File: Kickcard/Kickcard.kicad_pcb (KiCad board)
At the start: 2 copper layers, 135.3 x 114.8 mm, 74 parts, among them J1 Conn_Side_Expansion, SW1 SW_DIP_x04, SW2 SW_MEC_5E, SW3 SW_MEC_5E, U1 PAL20L8, U2 SST39SF040, U3 SST39SF040, U4 27C400

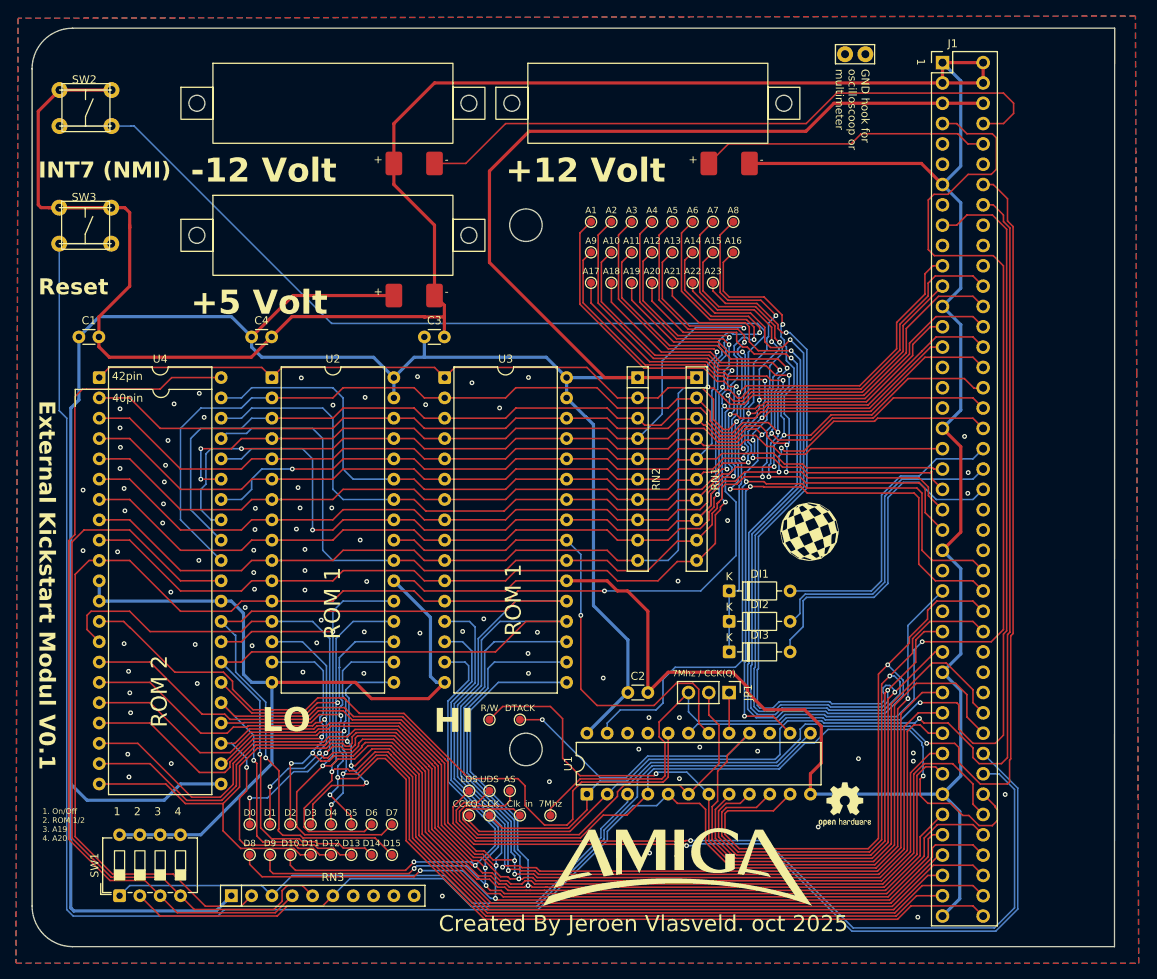
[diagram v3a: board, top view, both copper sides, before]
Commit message: Big Design change
Remove test pins, extra rom and added "expansion" headers, corrected voltmeter footprint dimmensions
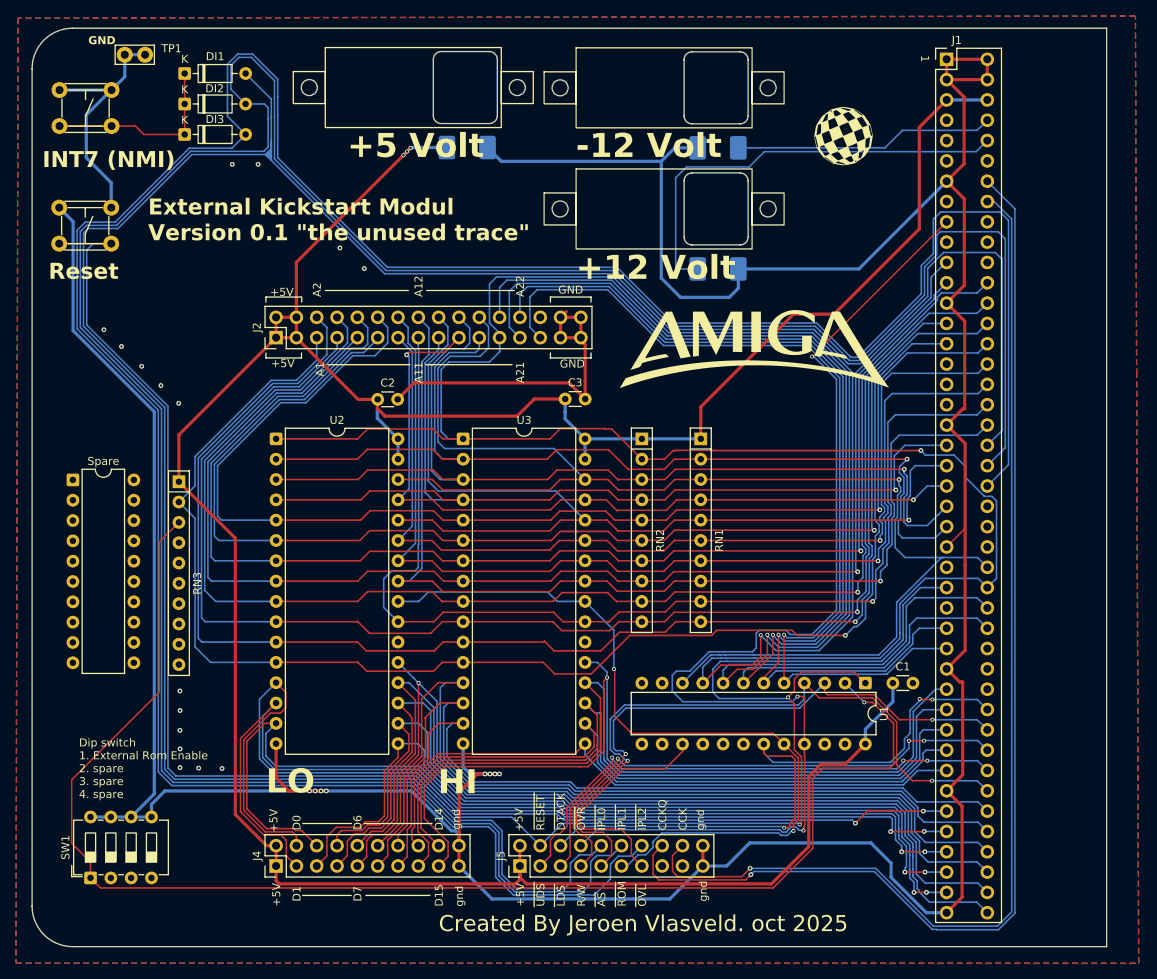
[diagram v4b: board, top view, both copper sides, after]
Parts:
- removed 7Mhz, A1, A10, A11, A12, A13, A14, A15, A16, A17, A18, A19, A2, A20, A21, A22, A23, A3, A4, A5, A6, A7, A8, A9, AS, CCK, CCKQ, Clk_in, D0, D1, D10, D11, D12, D13, D14, D15, D2, D3, D4, D5, D6, D7, D8, D9, DTACK, LDS, R/W, UDS: Conn_01x01, TestPoint:TestPoint_Pad_D1.0mm
- removed C4: 100nf, Capacitor_THT:C_Disc_D3.0mm_W1.6mm_P2.50mm
- removed JP1: Jumper_3_Open, Connector_PinHeader_2.54mm:PinHeader_1x03_P2.54mm_Vertical
- removed REF**: TestPoint_Bridge_Pitch2.54mm_Drill1.0mm, TestPoint:TestPoint_Bridge_Pitch2.54mm_Drill1.0mm
- removed REF**: OSHW-Logo2_7.3x6mm_SilkScreen, Symbol:OSHW-Logo2_7.3x6mm_SilkScreen
- removed U4: 27C400, Package_DIP:DIP-42_W15.24mm
- added J2: Conn_02x16_Odd_Even, Connector_PinHeader_2.54mm:PinHeader_2x16_P2.54mm_Vertical, F.Cu at (106.7, 75.4)
- added J4: Conn_02x10, Connector_PinHeader_2.54mm:PinHeader_2x10_P2.54mm_Vertical, F.Cu at (106.7, 141.5)
- added J5: Conn_02x10, Connector_PinHeader_2.54mm:PinHeader_2x10_P2.54mm_Vertical, F.Cu at (137.2, 141.5)
- added Spare: DIP-20_W7.62mm, Package_DIP:DIP-20_W7.62mm, F.Cu at (81.3, 93.2)
- added TP1: Conn_01x01, TestPoint:TestPoint_Bridge_Pitch2.54mm_Drill1.0mm, F.Cu at (87.8, 40.1)
- U1: value PAL20L8 -> GAL22v10
- moved C1 110.6 mm to (183.8, 118.6)
- moved DI1 93.9 mm to (95.2, 42.4)
- moved DI2 93.9 mm to (95.2, 46.2)
- moved DI3 93.9 mm to (95.2, 50.0)
- moved G*** 65.5 mm to (166.5, 76.8)
- moved RN3 52.2 mm to (94.5, 93.4), turned to -90 degrees
- moved G*** 49.6 mm to (177.6, 50.2)
- moved C2 48.2 mm to (119.4, 83.1)
- moved MES3 41.4 mm to (155.2, 44.2)
- moved U1 37.5 mm to (180.3, 118.6), turned to -90 degrees
- moved MES1 21.0 mm to (123.8, 44.2)
- moved C3 19.2 mm to (142.8, 83.1)
- moved MES2 13.4 mm to (155.2, 59.3)
- moved U3 8.00 mm to (130.1, 88.1)
- moved U2 7.68 mm to (106.7, 88.1)
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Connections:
- J1 pad 7: 7MHz -> unconnected-(J1-7MHz_or_NC-Pad7)
- RN3 pad 4: SW19 -> unconnected-(RN3-R3-Pad4)
- RN3 pad 5: SW20 -> unconnected-(RN3-R4-Pad5)
- RN3 pad 6: ROM_SEL -> unconnected-(RN3-R5-Pad6)
- SW1 pad 2: ROM_SEL -> unconnected-(SW1-Pad2)
- SW1 pad 3: SW19 -> unconnected-(SW1-Pad3)
- SW1 pad 4: SW20 -> unconnected-(SW1-Pad4)
- U1 pad 1: CCK -> RESET
- U1 pad 10: A21 -> A18
- U1 pad 11: A20 -> unconnected-(U1-I-Pad11)
- U1 pad 13: ROM_SEL -> unconnected-(U1-I-Pad13)
- U1 pad 14: A19 -> unconnected-(U1-I/O/Q-Pad14)
- U1 pad 15: unconnected-(U1-~{O_{1}}-Pad15) -> OVL
- U1 pad 16: DTACK -> unconnected-(U1-I/O/Q-Pad16)
- U1 pad 17: CLK_OUT -> unconnected-(U1-I/O/Q-Pad17)
- U1 pad 18: ROM1_EN -> unconnected-(U1-I/O/Q-Pad18)
- U1 pad 19: OVR -> DTACK
- U1 pad 2: CCKQ -> SW_KICK
- U1 pad 20: ROM2_EN -> ROM_EN
- U1 pad 21: unconnected-(U1-I/~{O_{7}}-Pad21) -> OVR
- U1 pad 23: A18 -> unconnected-(U1-I/O/Q-Pad23)
- U1 pad 3: SW_KICK -> R/W
- U1 pad 5: RESET -> A23
- U1 pad 6: CLK_IN -> A22
- U1 pad 7: R/W -> A21
- U1 pad 8: A23 -> A20
- U1 pad 9: A22 -> A19
- U2 pad 24: ROM1_EN -> ROM_EN
- U3 pad 24: ROM1_EN -> ROM_EN
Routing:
- net IPL2: track 43.9 -> 347.7 mm
- net IPL1: track 39.5 -> 342.4 mm
- net IPL0: track 37.8 -> 315.0 mm
- net 7MHz: track 163.3 -> 0.00 mm, vias 1 -> 0
- net Net-(DI1-K): track 141.6 -> 23.7 mm
- net D10: track 205.2 -> 96.6 mm, vias 2 -> 0
- net SW19: track 107.5 -> 0.00 mm
- net D11: track 191.4 -> 83.9 mm, vias 1 -> 0
- net SW_KICK: track 73.9 -> 176.7 mm, vias 0 -> 1
- net ROM_SEL: track 99.1 -> 0.00 mm
- net ROM_EN: track 0.00 -> 98.7 mm, vias 0 -> 2
- net D15: track 208.5 -> 110.1 mm, vias 2 -> 1
- net D14: track 199.2 -> 103.5 mm, vias 2 -> 0
- net ROM2_EN: track 95.5 -> 0.00 mm
- net D13: track 194.5 -> 99.0 mm, vias 3 -> 0
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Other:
- board size 135.3 x 114.8 mm -> 134.3 x 114.8 mm
- board text added: "+5V"
- board text added: "A1"
- board text added: "A11"
- board text added: "A12"
- board text added: "A2"
- board text added: "A21"
- board text added: "A22"
- board text added: "AS"
- board text added: "CCK"
- board text added: "CCKQ"
- board text added: "D0"
- board text added: "D1"
- board text added: "D14"
- board text added: "D15"
- board text added: "D6"
- board text added: "D7"
- board text added: "DTACK"
- board text added: "Dip switch 1. External Rom Enable 2. spare 3. spare 4. spare"
- board text added: "External Kickstart Modul Version 0.1 {dblquote}the unused trace{dblquote}"
- board text added: "GND"
- board text added: "IPL0"
- board text added: "IPL1"
- board text added: "IPL2"
- board text added: "LDS"
- board text added: "OVL"
- board text added: "OVR"
- board text added: "R/W"
- board text added: "RESET"
- board text added: "ROM"
- board text added: "UDS"
- board text added: "gnd"
- board text removed: "1"
- board text removed: "1. On/Off 2. ROM 1/2 3. A19 4. A20"
- board text removed: "2"
- board text removed: "3"
- board text removed: "4"
- board text removed: "40pin"
- board text removed: "42pin"
- board text removed: "7Mhz / CCK(Q)"
- board text removed: "External Kickstart Modul V0.1"
- board text removed: "GND hook for oscilloscoop or multimeter"
- board text removed: "ROM 1"
- board text removed: "ROM 2"
- board text removed: "dip switch: 1. On/Off 2. ROM 1/2 3. A19 4. A20"

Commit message: small update of track layout so gnd plane is better
small update of track layout so gnd plane is better
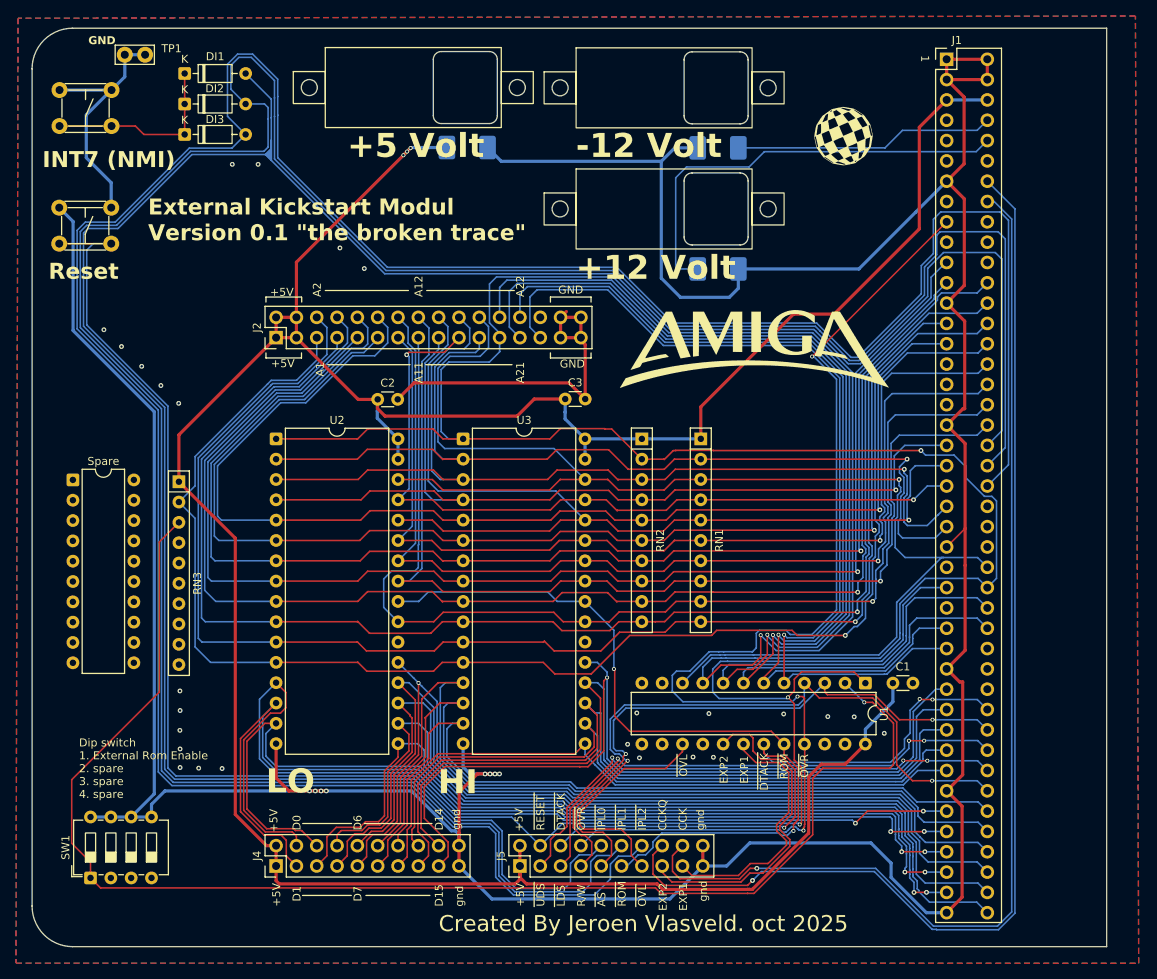
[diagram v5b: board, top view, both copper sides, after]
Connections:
- J5 pad 15: unconnected-(J5-Pin_15-Pad15) -> EXP2
- J5 pad 17: unconnected-(J5-Pin_17-Pad17) -> EXP1
- U1 pad 17: unconnected-(U1-I/O/Q-Pad17) -> EXP2
- U1 pad 18: unconnected-(U1-I/O/Q-Pad18) -> EXP1
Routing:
- net EXP2: track 0.00 -> 42.1 mm
- net EXP1: track 0.00 -> 32.9 mm
- net DTACK: track 79.6 -> 78.6 mm
- net CCKQ: track 146.8 -> 147.4 mm
- net GND: vias 24 -> 34
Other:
- board text added: "EXP1"
- board text added: "EXP2"
- board text added: "External Kickstart Modul Version 0.1 {dblquote}the broken trace{dblquote}"
- board text removed: "External Kickstart Modul Version 0.1 {dblquote}the unused trace{dblquote}"

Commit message: added fixing holes
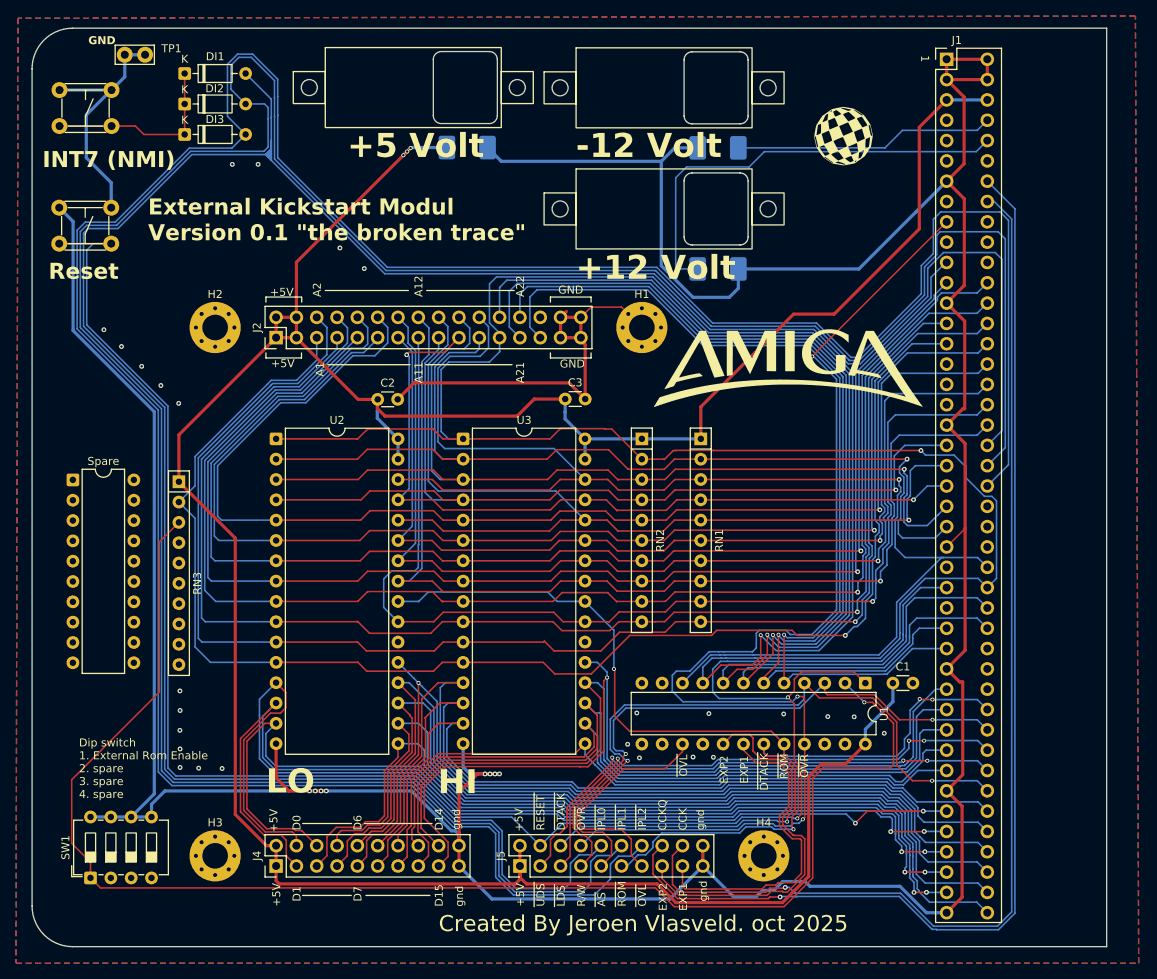
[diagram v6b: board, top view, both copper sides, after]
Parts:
- added H1: MountingHole_Pad, MountingHole:MountingHole_3.2mm_M3_Pad_Via, F.Cu at (152.4, 74.2)
- added H2: MountingHole_Pad, MountingHole:MountingHole_3.2mm_M3_Pad_Via, F.Cu at (99.1, 74.2)
- added H3: MountingHole_Pad, MountingHole:MountingHole_3.2mm_M3_Pad_Via, F.Cu at (99.1, 140.2)
- added H4: MountingHole_Pad, MountingHole:MountingHole_3.2mm_M3_Pad_Via, F.Cu at (167.6, 140.2)
- moved G*** 4.87 mm to (170.7, 79.2)
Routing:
- net EXP1: track 32.9 -> 40.7 mm
- net GND: track 537.7 -> 544.1 mm
- net EXP2: track 42.1 -> 48.5 mm
- net SW_KICK: track 176.2 -> 180.8 mm
- net +5V: track 356.7 -> 361.3 mm
- net OVR: track 147.6 -> 146.3 mm
- net CCKQ: track 147.4 -> 146.2 mm
- net DTACK: track 78.6 -> 77.7 mm
- net D0: track 128.7 -> 129.4 mm
- net D11: track 83.9 -> 84.5 mm
- net D10: track 96.6 -> 97.2 mm
- net D8: track 113.5 -> 114.1 mm
- net D6: track 117.6 -> 118.2 mm
- net D7: track 118.3 -> 118.9 mm
- net D2: track 120.5 -> 121.1 mm
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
